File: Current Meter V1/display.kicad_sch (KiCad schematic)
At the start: 3 parts, among them J401 I2C OLED Display Connector

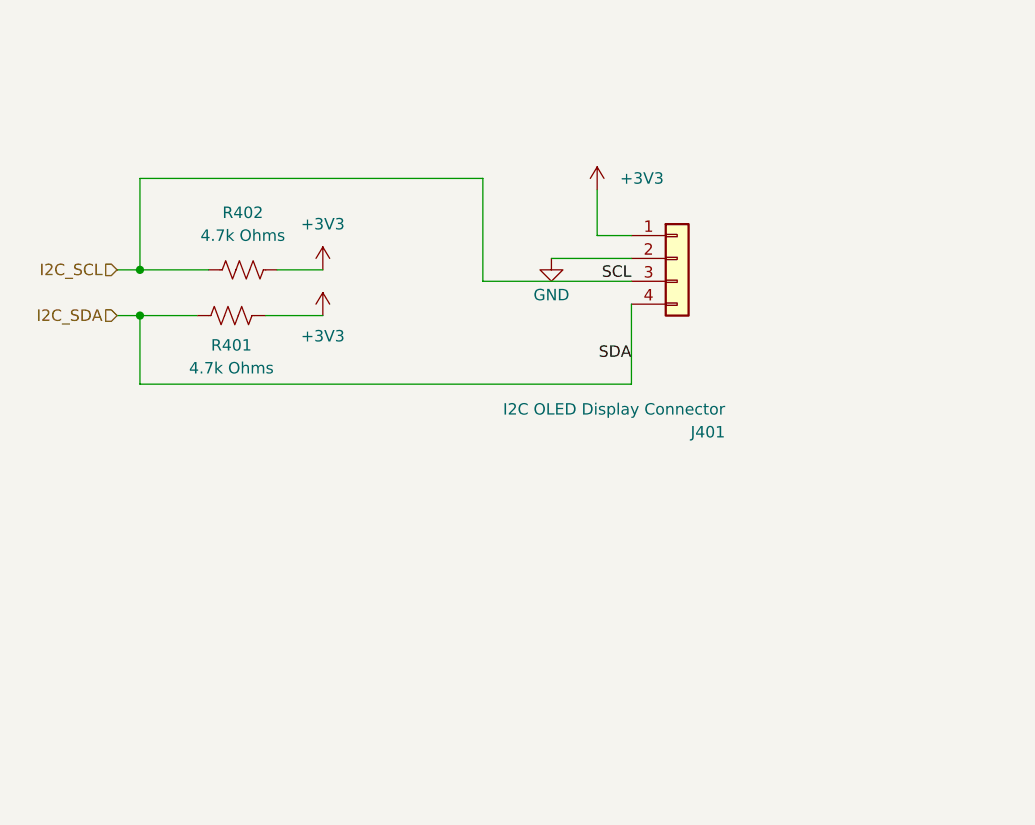
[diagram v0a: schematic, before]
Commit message: updated footprints
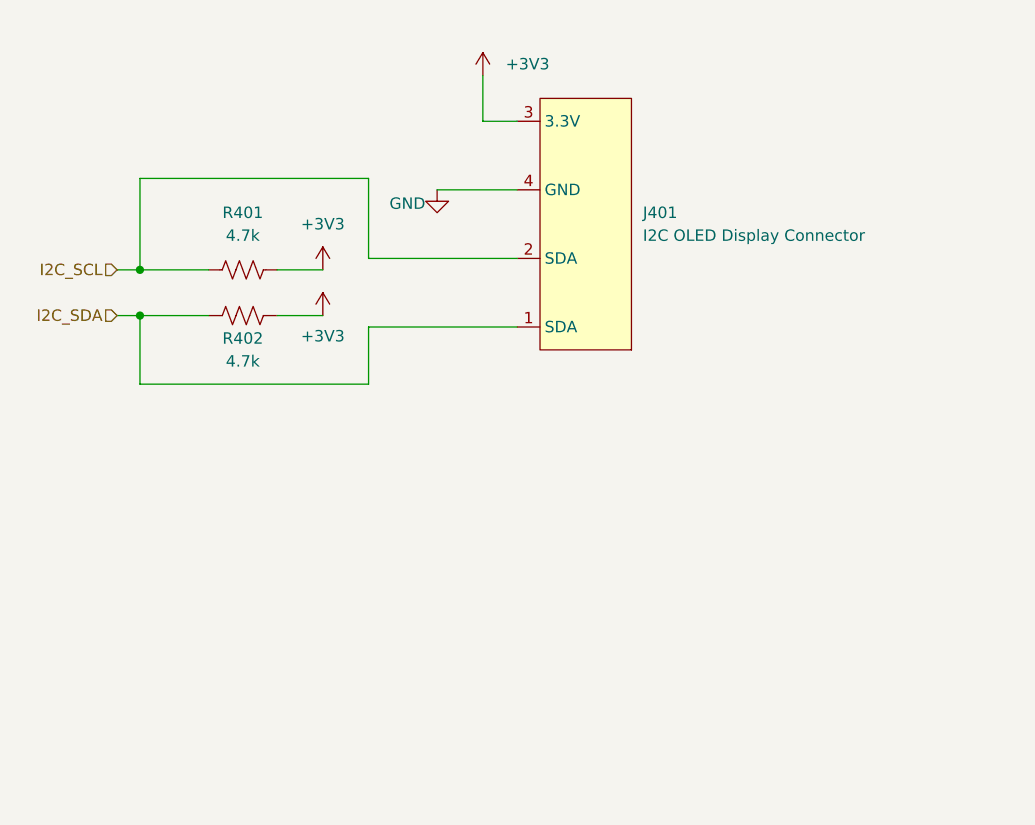
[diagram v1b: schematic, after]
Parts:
- removed J401: I2C OLED Display Connector, symbol Connector_Generic:Conn_01x04
- removed R401, R402: 4.7k Ohms, symbol Device:R_US
- added J401: I2C OLED Display Connector, Connector_Molex:Molex_Micro-Fit_3.0_43650-0400_1x04_P3.00mm_Horizontal, symbol bfr_connectors:DAQ_Connector
- added R401, R402: 4.7k, Resistor_SMD:R_0805_2012Metric_Pad1.20x1.40mm_HandSolder, symbol bfr_resistors:RMCF0805FT4K70
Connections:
- net +3V3: now also J401.3, R401.2, R402.2
- net GND: now also J401.4
- net I2C_SCL: now also J401.2, R401.1
- net I2C_SDA: now also J401.1, R402.1

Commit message: changed everything to 5V
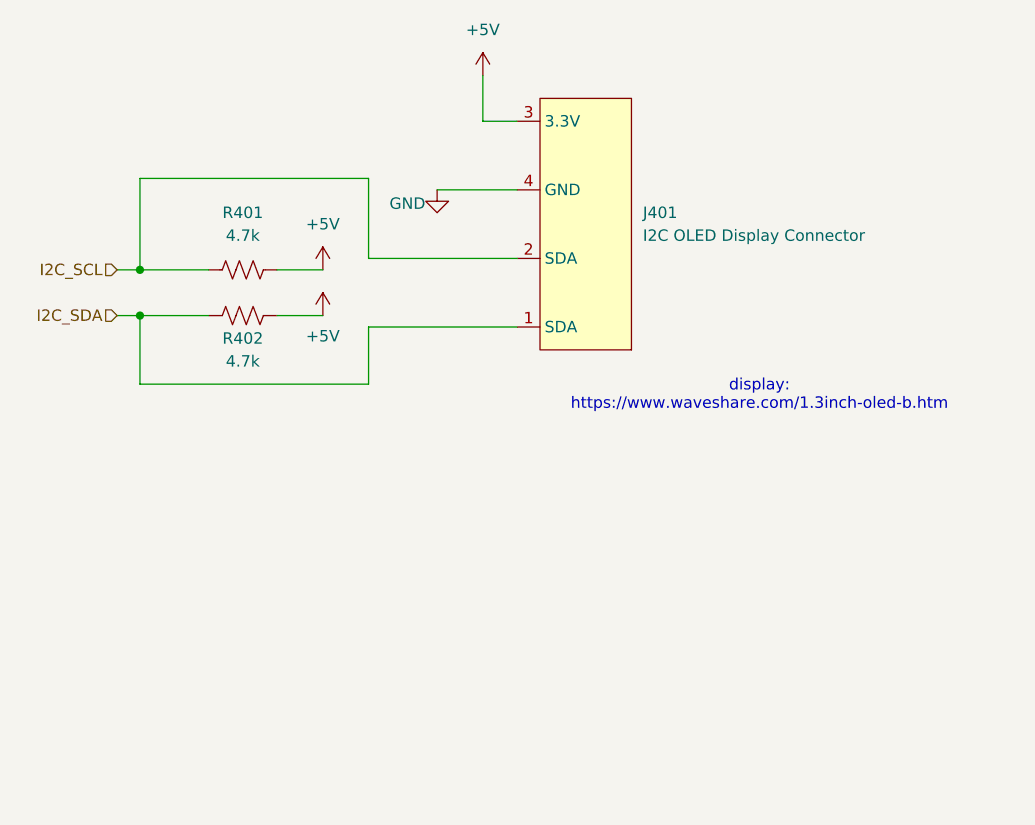
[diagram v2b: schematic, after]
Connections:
- net +3V3 renamed +5V
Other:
- note added: "display: https://www.waveshare.com/1.3inch-oled-b.htm"
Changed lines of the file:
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@@
 	(generator_version "9.0")
 	(paper "A4")
+	(text "display: \nhttps://www.waveshare.com/1.3inch-oled-b.htm"
+		(exclude_from_sim no)
+		(at 159.004 105.41 0)
+		(effects
+			(font
+				(size 1.27 1.27)
+			)
+		)
+	)
 	(junction
 		(at 90.17 91.44)
@@
 			)
 		)
-		(property "Value" "+3V3"
-			(at 130.81 68.5799 0)
-			(effects
-				(font
-					(size 1.27 1.27)
-				)
-				(justify left)
+		(property "Value" "+5V"
+			(at 128.27 64.77 0)
+			(effects
+				(font
+					(size 1.27 1.27)
+				)
 			)
 		)
@@
 			)
 		)
-		(property "Value" "+3V3"
+		(property "Value" "+5V"
 			(at 110.49 86.36 0)
 			(effects
@@
 			)
 		)
-		(property "Value" "+3V3"
+		(property "Value" "+5V"
 			(at 110.49 98.806 0)
 			(effects

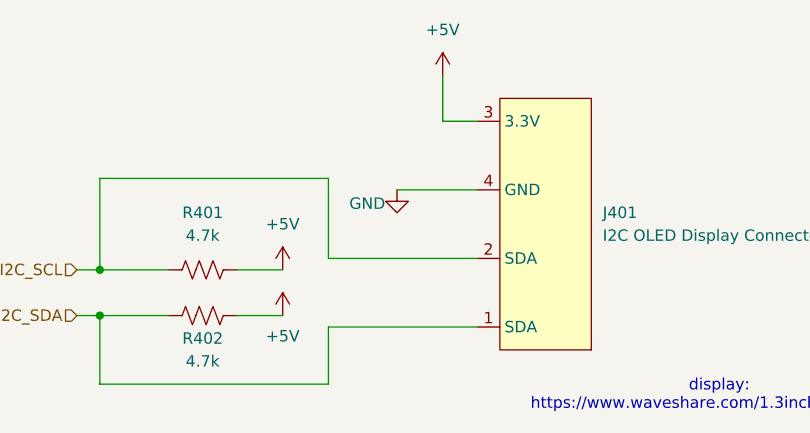
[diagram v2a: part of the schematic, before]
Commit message: updated layout
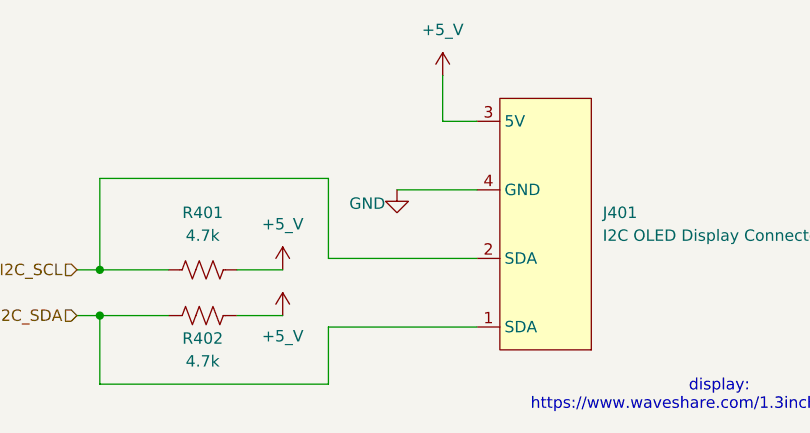
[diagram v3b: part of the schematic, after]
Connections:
- net +5V renamed +5_V
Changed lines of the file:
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@@
 			)
 		)
-		(property "Value" "+5V"
+		(property "Value" "+5_V"
 			(at 128.27 64.77 0)
 			(effects
@@
 			)
 		)
-		(property "Value" "+5V"
+		(property "Value" "+5_V"
 			(at 110.49 86.36 0)
 			(effects
@@
 			)
 		)
-		(property "Value" "+5V"
+		(property "Value" "+5_V"
 			(at 110.49 98.806 0)
 			(effects
@@
 		)
 		(pin "3"
-			(alternate "3.3V")
+			(alternate "5V")
 		)
 		(pin "2"

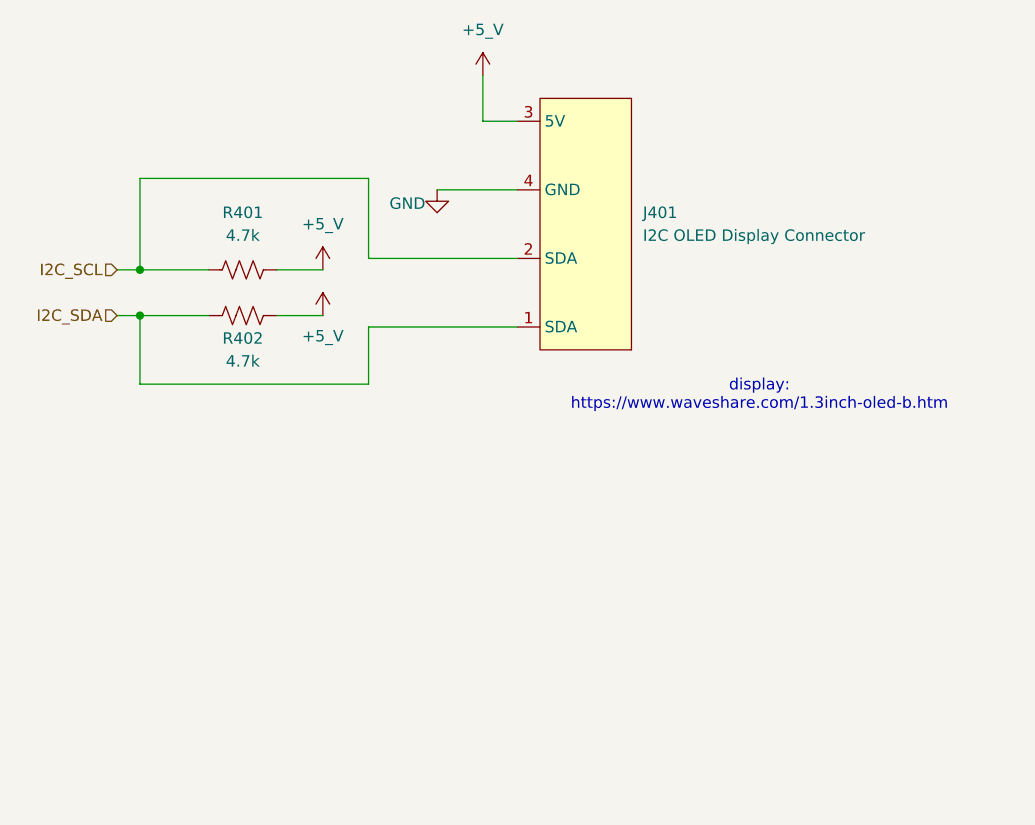
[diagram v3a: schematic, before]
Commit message: added sensor connector, updated pcb layout
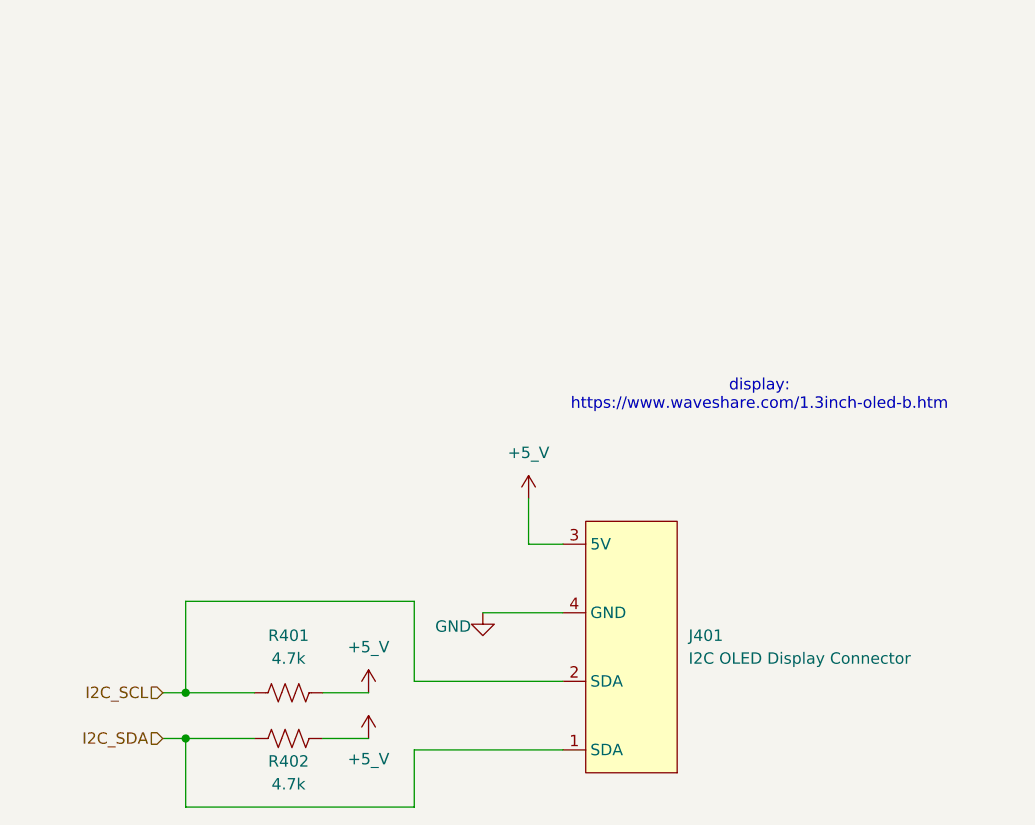
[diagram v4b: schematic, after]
